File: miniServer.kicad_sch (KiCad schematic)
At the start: 5 parts, among them U1 STM32H725VGTx

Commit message: Added MCU power connections
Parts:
- added C18, C19: 2.2uF, symbol Device:C_Small
- added C20, C21, C22, C23, C24, C25, C26, C27, C28, C29, C30, C31, C32, C33, C34, C35: 100nF, symbol Device:C_Small
- added C36, C37: 4.7uF, symbol Device:C_Small
- added R32: 47R, symbol Device:R
- added R34: 10kR, symbol Device:R
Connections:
- net at U1.100 (VDD): now also U1.20 (VDD), U1.24 (VDDA), U1.30 (VDD), U1.4 (VDD), U1.46 (VDDLDO), U1.47 (VDD), U1.5 (VBAT), U1.59 (VDD), U1.74 (VDDLDO), U1.75 (VDD), U1.76 (VDD33USB), U1.88 (VDD), U1.99 (VDDLDO), C21.1, C22.1, C23.1, C24.1, C25.1, C26.1, C27.1, C28.1, C29.1, C30.1, C31.1, C32.1, C33.1, C34.1, C35.1, C36.1, C37.1, R32.1
- net GND: now reaches U1.11 (VDDSMPS)
- net GND: now also U1.12 (VFBSMPS), U1.21 (VSS), U1.22 (VSSA), U1.29 (VSS), U1.45 (VSS), U1.58 (VSS), U1.73 (VSS), U1.9 (VSSSMPS), U1.98 (VSS), C18.2, C19.2, C20.2, C21.2, C22.2, C23.2, C24.2, C25.2, C26.2, C27.2, C28.2, C29.2, C30.2, C31.2, C32.2, C33.2, C34.2, C35.2, C36.2, C37.2, R34.2
- net nRST: now reaches U1.15 (NRST)
- net nRST: now also C20.1
- net at U1.23 (VREF+): now also R32.2
- net at U1.44 (VCAP): now also U1.72 (VCAP), U1.97 (VCAP), C18.1, C19.1
- net at U1.94 (BOOT0): now also R34.1
- no-connect marks 0 -> 1
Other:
- sheet Ethernet ports: added ETH_CRS_DV, ETH_MDC, ETH_MDIO, ETH_REF_CLK, ETH_RXD0, ETH_RXD1, ETH_RXER, ETH_TXD0, ETH_TXD1, ETH_TXEN, ETH_nINT, ETH_nRST; removed none
- sheet SDMMC ports: added SDMMC_CLK, SDMMC_CMD, SDMMC_DAT0, SDMMC_DAT1, SDMMC_DAT2, SDMMC_DAT3, SDMMC_nDET; removed none
- sheet USB ports: added USB_DN, USB_DP; removed none
- moved on the sheet: H1, H2, H3, H4, U1

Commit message: Started with pin mapping
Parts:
- added C16, C17: 10uF, Capacitor_SMD:C_0805_2012Metric_Pad1.18x1.45mm_HandSolder, symbol Device:C
- added J3: Conn_ARM_SWD_TagConnect_TC2030-NL, Connector:Tag-Connect_TC2030-IDC-NL_2x03_P1.27mm_Vertical, symbol Connector:Conn_ARM_SWD_TagConnect_TC2030-NL
- added R33: 10kR, Resistor_SMD:R_0805_2012Metric_Pad1.20x1.40mm_HandSolder, symbol Device:R
- added U4: LT1963AxST-3.3, Package_TO_SOT_SMD:SOT-223-3_TabPin2, symbol Regulator_Linear:LT1963AxST-3.3
- C18, C19, C20, C21, C22, C23, C24, C25, C26, C27, C28, C29, C30, C31, C32, C33, C34, C35, C36, C37: footprint (none) -> Capacitor_SMD:C_0805_2012Metric_Pad1.18x1.45mm_HandSolder
- R32, R34: footprint (none) -> Resistor_SMD:R_0805_2012Metric_Pad1.20x1.40mm_HandSolder
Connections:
- net GND: now also C16.2, C17.2, J3.5 (GND), U4.2 (GND)
- net USB/USB_DN: now also U1.69 (PA11)
- net USB/USB_DP: now also U1.68 (PA10)
- net nRST: now also J3.3 (~{RESET})
- net +3V3: now reaches C21.1, C22.1, C23.1, C24.1, C25.1, C26.1, C27.1, C28.1, C29.1, C30.1, C31.1, C32.1, C33.1, C34.1, C35.1, C36.1, C37.1, R32.1, U1.100 (VDD), U1.20 (VDD), U1.24 (VDDA), U1.30 (VDD), U1.4 (VDD), U1.46 (VDDLDO), U1.47 (VDD), U1.5 (VBAT), U1.59 (VDD), U1.74 (VDDLDO), U1.75 (VDD), U1.76 (VDD33USB), U1.88 (VDD), U1.99 (VDDLDO)
- net +3V3: now also C17.1, J3.1 (VCC), R33.2, U4.3 (OUT)
- net RCC_OSC_IN: now reaches U1.13 (PH0)
- net RCC_OSC_OUT: now reaches U1.14 (PH1)
- net ETH_MDC: now reaches U1.17 (PC1)
- net WKUP1: now reaches U1.25 (PA0)
- net WKUP1: now also R33.1
- net ETH_REF_CLK: now reaches U1.26 (PA1)
- net ETH_MDIO: now reaches U1.27 (PA2)
- net ETH_CRS_DV: now reaches U1.34 (PA7)
- net ETH_RXD0: now reaches U1.35 (PC4)
- net ETH_RXD1: now reaches U1.36 (PC5)
- net ETH_TX_EN: now reaches U1.43 (PB11)
- net ETH_TXD0: now reaches U1.48 (PB12)
- net ETH_TXD1: now reaches U1.49 (PB13)
- net ETH_nINT: now reaches U1.6 (PC13)
- net SDMMC_D0: now reaches U1.62 (PC6)
- net SDMMC_D0: now also U1.64 (PC8)
- net SDMMC_D1: now reaches U1.63 (PC7)
- net SDMMC_D1: now also U1.65 (PC9)
- net DEBUG_SWIO: now reaches U1.71 (PA13(JTMS)
- net DEBUG_SWIO: now also J3.2 (SWDIO)
- net DEBUG_SWCLK: now reaches U1.77 (PA14(JTCK)
- net DEBUG_SWCLK: now also J3.4 (SWCLK)
- net SDMMC_D2: now reaches U1.79 (PC10)
- net SDMMC_D3: now reaches U1.80 (PC11)
- net SDMMC_CK: now reaches U1.81 (PC12)
- net SDMMC_CK: now also U1.95 (PB8)
- net SDMMC_CMD: now reaches U1.84 (PD2)
- net DEBUG_SWO: now reaches U1.89 (PB3(JTDO)
- net DEBUG_SWO: now also J3.6 (SWO)
- new net +4V: C16.1, U4.1 (IN)
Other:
- removed sheet Power
- note added: "DEBUG"
- note added: "Power"

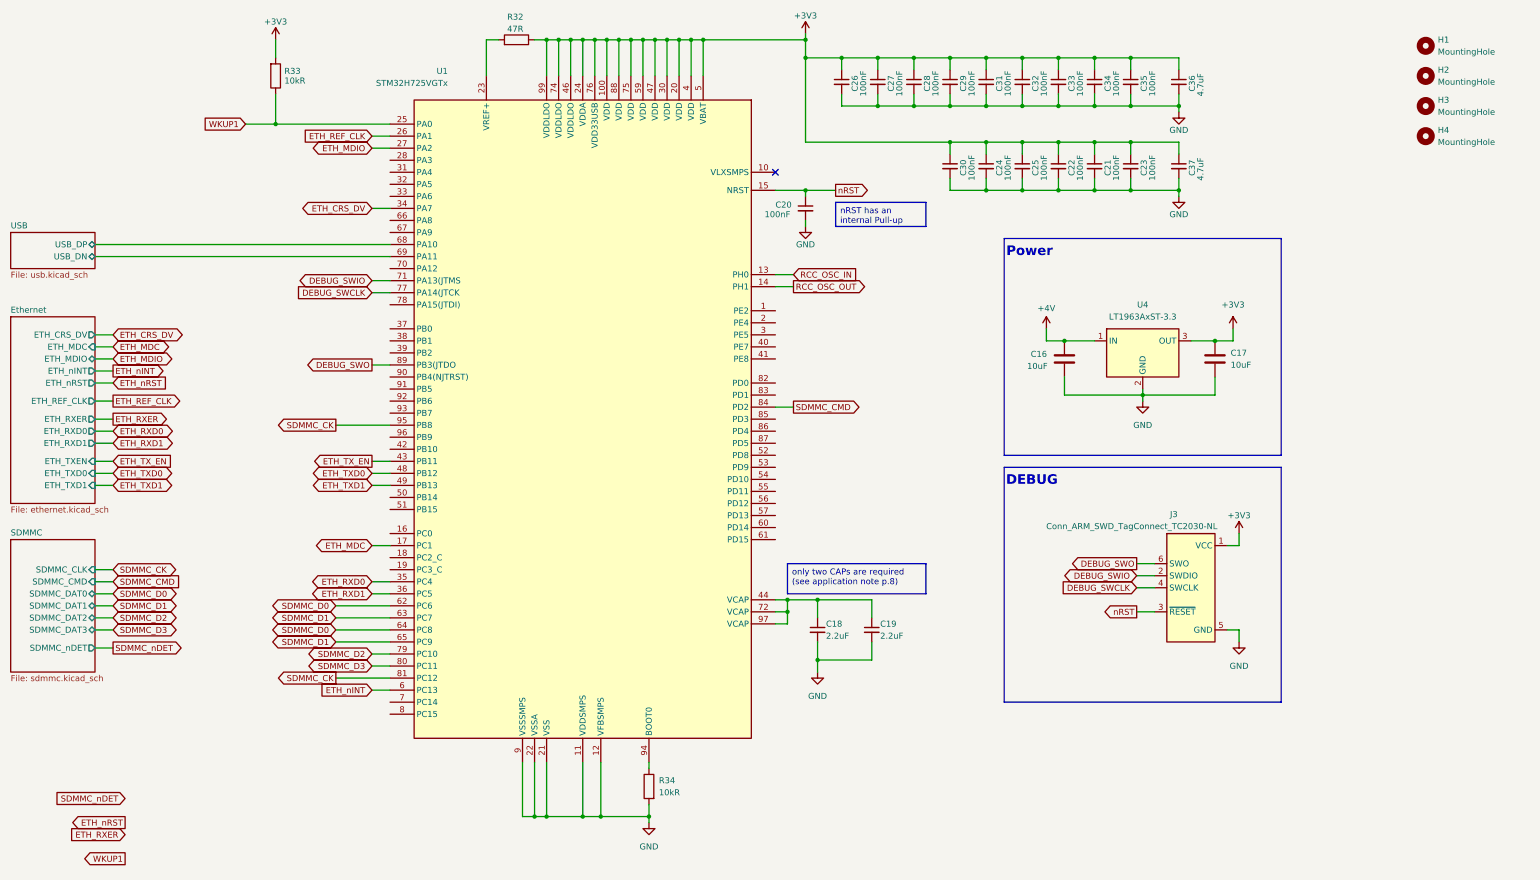
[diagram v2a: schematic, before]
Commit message: Added 48MHz quartz
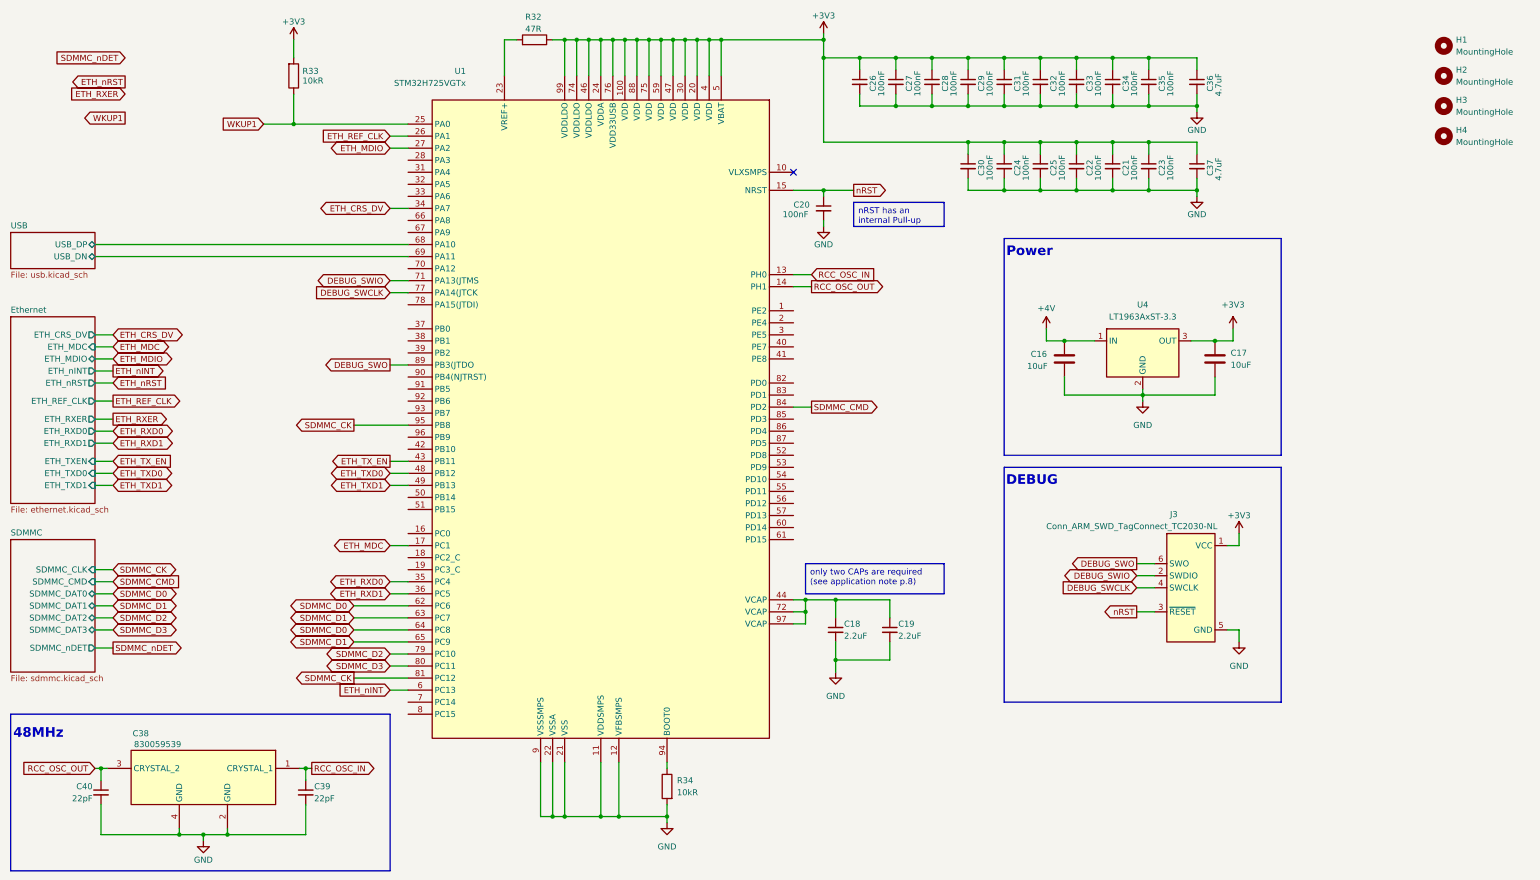
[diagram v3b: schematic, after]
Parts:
- added C38: 830059539, 830059539, symbol 830059539:830059539
- added C39, C40: 22pF, Capacitor_SMD:C_0805_2012Metric_Pad1.18x1.45mm_HandSolder, symbol Device:C_Small
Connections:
- net GND: now also C38.2 (GND), C38.4 (GND), C39.2, C40.2
- net RCC_OSC_IN: now also C38.1 (CRYSTAL_1), C39.1
- net RCC_OSC_OUT: now also C38.3 (CRYSTAL_2), C40.1
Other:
- note added: "48MHz"
- moved on the sheet: C18, C19, C20, C21, C22, C23, C24, C25, C26, C27, C28, C29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

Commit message: layout v1
no silkscreen done yet
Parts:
- removed C24, C28, C29, C30, C31, C32: 100nF, Capacitor_SMD:C_0805_2012Metric_Pad1.18x1.45mm_HandSolder, symbol Device:C_Small
- removed U4: LT1963AxST-3.3, Package_TO_SOT_SMD:SOT-223-3_TabPin2, symbol Regulator_Linear:LT1963AxST-3.3
- added J10: Conn_01x01, Connector_Wire:SolderWirePad_1x01_SMD_1.5x3mm, symbol Connector_Generic:Conn_01x01
- added U5: NCP1117-3.3_SOT223, Package_TO_SOT_SMD:SOT-223-3_TabPin2, symbol Regulator_Linear:NCP1117-3.3_SOT223
- C34, C35: value 100nF -> 4.7uF
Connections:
- net +3V3: now also U5.2 (VO)
- net +4V: now also U5.3 (VI)
- net DEBUG_SWIO: now also U1.67 (PA9)
- net ETH_nRST: now also U1.50 (PB14)
- net GND: now also U5.1 (GND)
- net SDMMC_CK: now also U1.78 (PA15(JTDI)); no longer U1.95 (PB8)
- net SDMMC_D0: no longer U1.62 (PC6)
- net SDMMC_D1: no longer U1.63 (PC7)
- net SDMMC_nDET: now also U1.82 (PD0)
- net WKUP1: now also J10.1 (Pin_1)
- net USB_DP: now reaches U1.70 (PA12)
- net USB/USB_DN renamed USB_DN
- net USB/USB_DP: no longer names the net of U1.68 (PA10)
- no-connect marks 1 -> 2
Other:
- note added: "Wakeup"
- moved on the sheet: C21, C22, C23, C25, C26, C27, C33, C34, C35, C36, C37

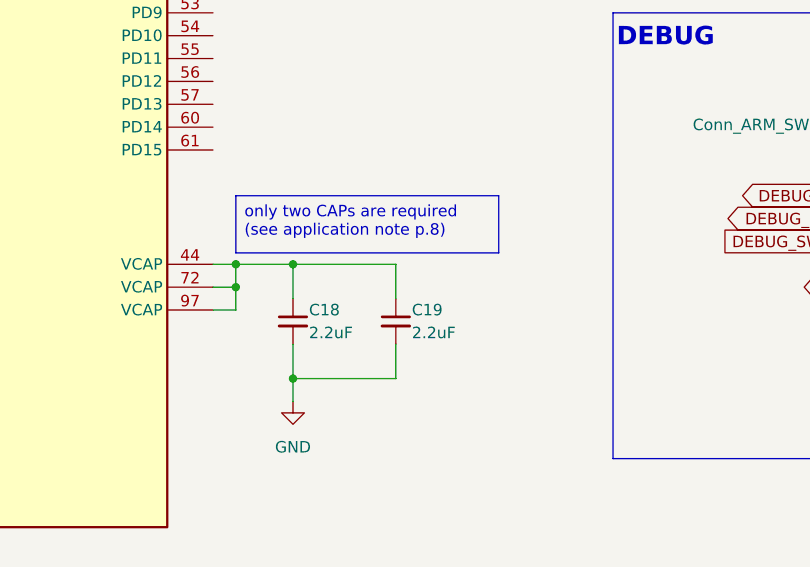
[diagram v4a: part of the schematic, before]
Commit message: Changed comment on VCAPs of MCU + added pdf link for our configuration
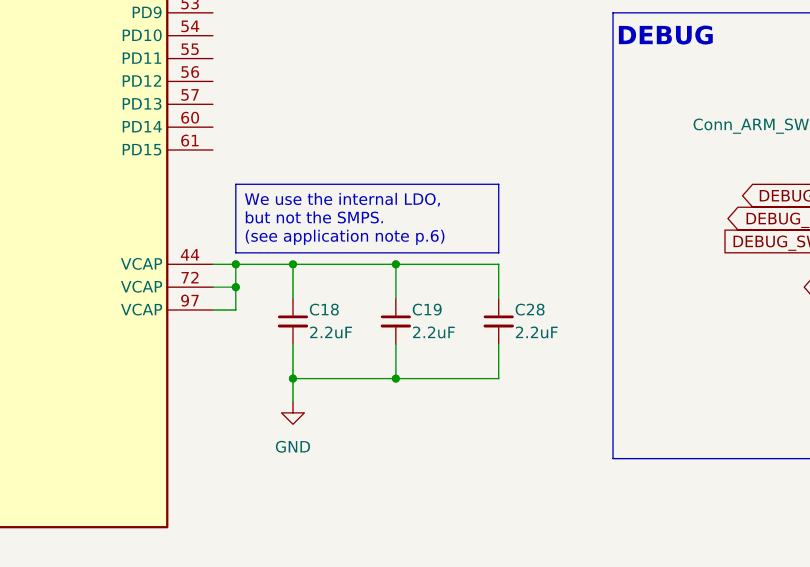
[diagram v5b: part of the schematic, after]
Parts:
- added C28: 2.2uF, Capacitor_SMD:C_0805_2012Metric_Pad1.18x1.45mm_HandSolder, symbol Device:C_Small
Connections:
- net GND: now also C28.2
- net at C18.1, C19.1, U1.44 (VCAP)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: now also C28.1

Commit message: Changed ETH connector, cleared old layout
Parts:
- C38: footprint 830059539 -> KiCad:830059539
